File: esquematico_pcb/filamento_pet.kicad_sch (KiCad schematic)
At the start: 35 parts, among them P1 Digital, P2 Analog, P3 CONN_01X01, P4 CONN_01X01, P5 CONN_01X01, P6 CONN_01X01, Q1 IRF540N, Q2 IRF540N

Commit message: Footprints listos
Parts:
- removed J? (x3): Conn_01x02_Male, symbol filamento_pet-rescue:Conn_01x02_Male-Connector
- removed J? (x4): 01x02M, symbol filamento_pet-rescue:Conn_01x02_Male-Connector
- removed P3, P4, P5, P6: CONN_01X01, Socket_Arduino_Nano:1pin_Nano, symbol Connector_Generic:Conn_01x01
- added J1, J11, J13, J2, J4, J5, J8: 01x02M, TerminalBlock_4Ucon:TerminalBlock_4Ucon_1x02_P3.50mm_Horizontal, symbol filamento_pet-rescue:Conn_01x02_Male-Connector
- C1, C3: value CP1 -> 100uf; footprint (none) -> Capacitor_THT:CP_Radial_D8.0mm_P3.50mm
- C2: value CP1 -> 10uf; footprint (none) -> Capacitor_THT:CP_Radial_D8.0mm_P3.50mm
- D1, D2: footprint (none) -> LED_THT:LED_D5.0mm
- J10, J6, J7: renamed from J?; footprint (none) -> Connector_PinHeader_2.54mm:PinHeader_1x03_P2.54mm_Vertical
- J12, J9: renamed from J?; footprint (none) -> Connector_PinHeader_2.54mm:PinHeader_1x04_P2.54mm_Vertical
- J3: renamed from J?; footprint (none) -> TerminalBlock_4Ucon:TerminalBlock_4Ucon_1x02_P3.50mm_Horizontal
- P1, P2: footprint Socket_Arduino_Nano:Socket_Strip_Arduino_1x15 -> Connector_PinHeader_2.54mm:PinHeader_1x16_P2.54mm_Vertical
- R1, R2, R3, R4, R5, R6, R7: footprint (none) -> Resistor_THT:R_Axial_DIN0204_L3.6mm_D1.6mm_P7.62mm_Horizontal
- R8: value 10K -> R; footprint (none) -> Resistor_THT:R_Axial_DIN0204_L3.6mm_D1.6mm_P7.62mm_Horizontal
- gave numbers to parts that had none: 1
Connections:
- net +12V: now also J2.1 (Pin_1), J5.2 (Pin_2)
- net +5V: now also R7.2, R8.1; no longer R7.1, R8.2
- net BUT1: now also J8.2 (Pin_2)
- net BUT2: now also J11.2 (Pin_2)
- net BUT3: now also J13.2 (Pin_2)
- net EN: now also R8.2; no longer R8.1
- net FAN: now also R5.2; no longer R5.1
- net GND: now also R3.2, R6.2, J1.2 (Pin_2), J11.1 (Pin_1), J13.1 (Pin_1), J4.2 (Pin_2), J8.1 (Pin_1); no longer R3.1, R6.1
- net MOS: now also R2.2; no longer R2.1
- net Thermistor: now also R7.1, J4.1 (Pin_1); no longer R7.2
- net at D2.1 (K), Q2.2 (D): now also J5.1 (Pin_1)
- new net: Q1.1 (G), R2.1, R3.1
- new net: Q2.1 (G), R5.1, R6.1
- new net: J1.1 (Pin_1), J2.2 (Pin_2)
- no-connect marks 3 -> 0
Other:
- note removed: "Holes"

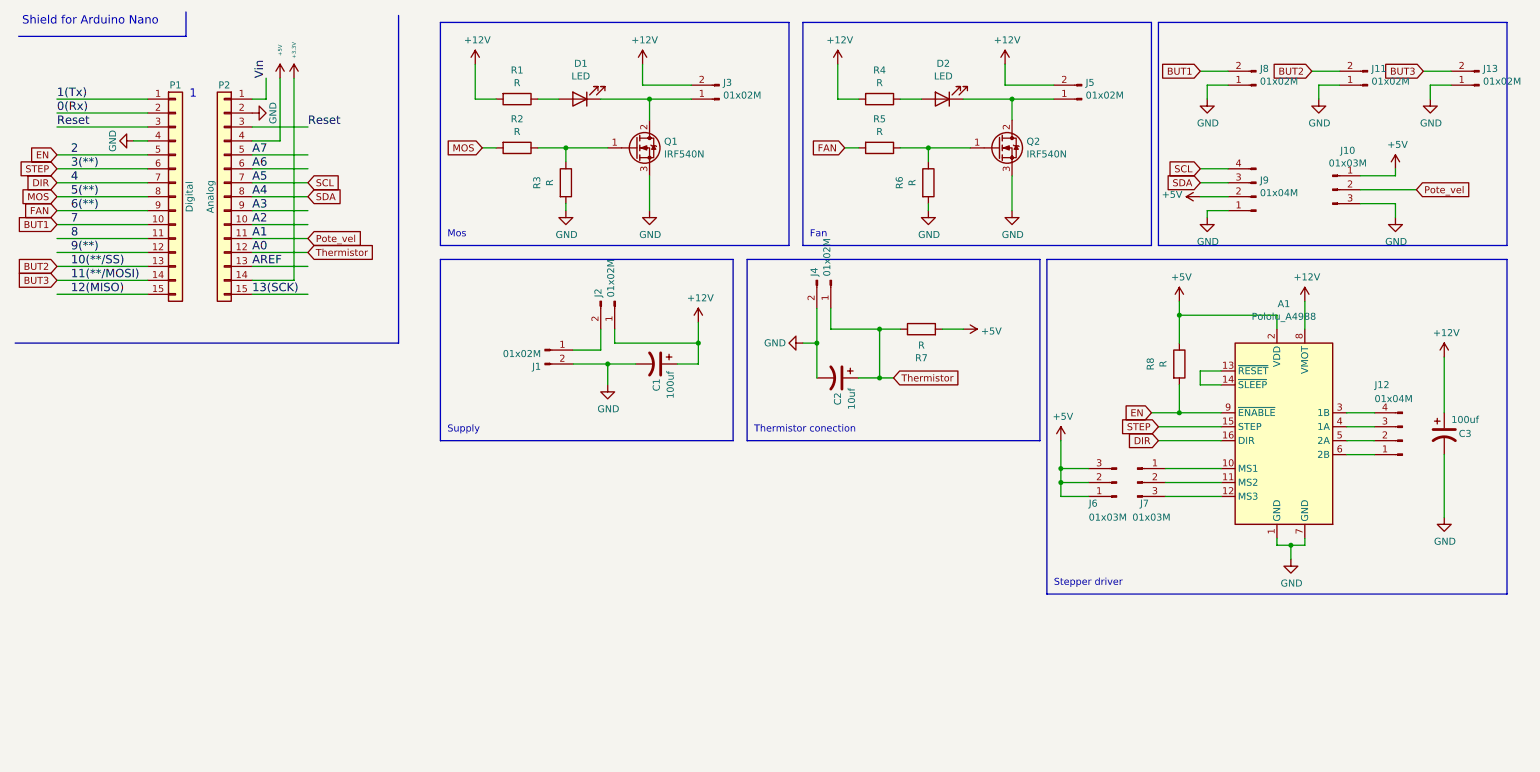
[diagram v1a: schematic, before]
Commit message: Cambio de footprint Arduino Nano. Conector para encoder (Opcional). 2 Botones
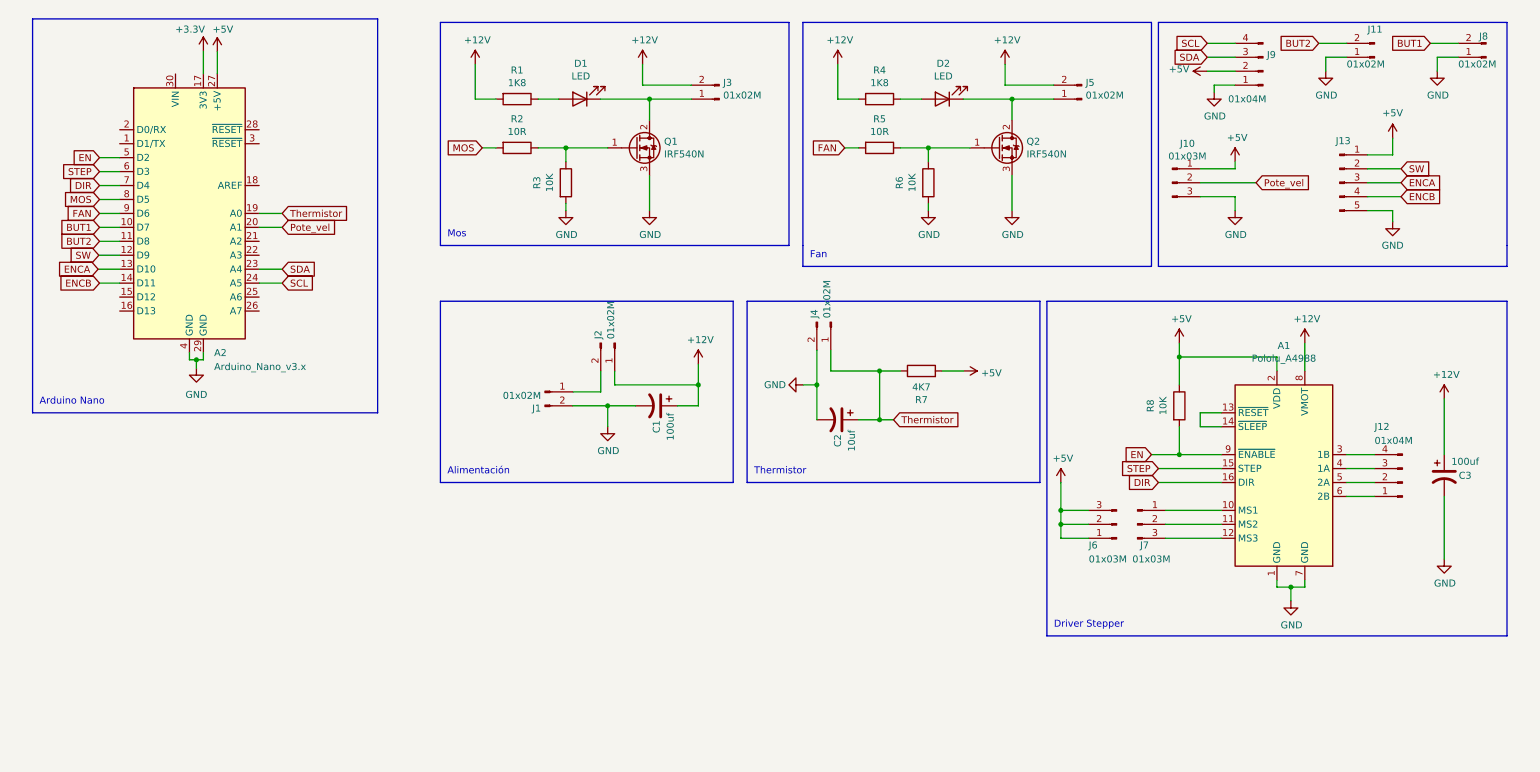
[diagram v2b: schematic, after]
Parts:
- removed J13: 01x02M, TerminalBlock_4Ucon:TerminalBlock_4Ucon_1x02_P3.50mm_Horizontal, symbol filamento_pet-rescue:Conn_01x02_Male-Connector
- removed P1: Digital, Connector_PinHeader_2.54mm:PinHeader_1x16_P2.54mm_Vertical, symbol Connector_Generic:Conn_01x15
- removed P2: Analog, Connector_PinHeader_2.54mm:PinHeader_1x16_P2.54mm_Vertical, symbol Connector_Generic:Conn_01x15
- added A2: Arduino_Nano_v3.x, Module:Arduino_Nano, symbol MCU_Module:Arduino_Nano_v3.x
- added J13: Conn_01x05_Pin, Connector_PinHeader_2.54mm:PinHeader_1x05_P2.54mm_Vertical, symbol Connector:Conn_01x05_Pin
- R1, R4: value R -> 1K8
- R2, R5: value R -> 10R
- R3, R6, R8: value R -> 10K
- R7: value R -> 4K7
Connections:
- net +5V: now also A2.27 (+5V), J13.1 (Pin_1)
- net BUT1: now also A2.10 (D7)
- net BUT2: now also A2.11 (D8)
- net DIR: now also A2.7 (D4)
- net EN: now also A2.5 (D2)
- net FAN: now also A2.9 (D6)
- net GND: now also A2.29 (GND), A2.4 (GND), J13.5 (Pin_5)
- net MOS: now also A2.8 (D5)
- net Pote_vel: now also A2.20 (A1)
- net SCL: now also A2.24 (A5)
- net SDA: now also A2.23 (A4)
- net STEP: now also A2.6 (D3)
- net Thermistor: now also A2.19 (A0)
- new net +3.3V: A2.17 (3V3)
- new net ENCA: A2.13 (D10), J13.3 (Pin_3)
- new net ENCB: A2.14 (D11), J13.4 (Pin_4)
- new net SW: A2.12 (D9), J13.2 (Pin_2)
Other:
- note added: "Alimentación"
- note added: "Arduino Nano"
- note added: "Driver Stepper"
- note added: "Thermistor"
- note removed: "1"
- note removed: "Shield for Arduino Nano"
- note removed: "Stepper driver"
- note removed: "Supply"
- note removed: "Thermistor conection"
- moved on the sheet: A1, C1, C2, C3, J1, J10, J11, J12, J2, J4, J6, J7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

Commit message: PCB V1.0.0
Agregué LM7805
Cambios pequeños en el esquemático
V1.0.0 del PCB
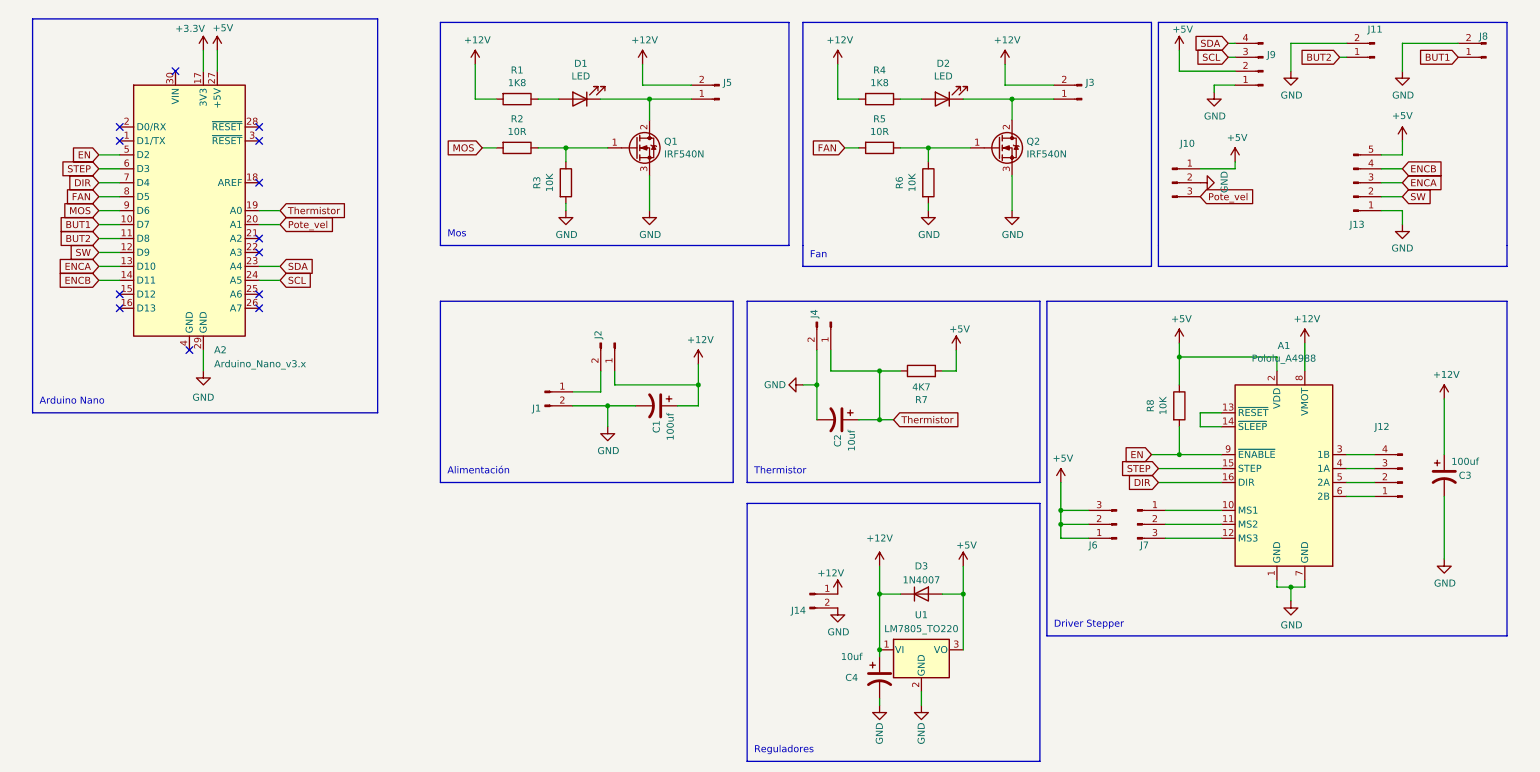
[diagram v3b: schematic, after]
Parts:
- added C4: 10uf, Capacitor_THT:CP_Radial_D8.0mm_P3.50mm, symbol filamento_pet-rescue:CP1-Device
- added D3: 1N4007, Diode_THT:D_DO-41_SOD81_P10.16mm_Horizontal, symbol Diode:1N4007
- added J14: 01x02M, TerminalBlock_4Ucon:TerminalBlock_4Ucon_1x02_P3.50mm_Horizontal, symbol filamento_pet-rescue:Conn_01x02_Male-Connector
- added U1: LM7805_TO220, Package_TO_SOT_THT:TO-220-3_Vertical, symbol Regulator_Linear:LM7805_TO220
- renumbered J5 to J3, J3 to J5
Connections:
- net +12V: now also C4.1, D3.1 (K), J14.1 (Pin_1), U1.1 (VI)
- net +5V: now also J13.5 (Pin_5), D3.2 (A), U1.3 (VO); no longer J13.1 (Pin_1)
- net BUT1: now also J8.1 (Pin_1); no longer J8.2 (Pin_2)
- net BUT2: now also J11.1 (Pin_1); no longer J11.2 (Pin_2)
- net FAN: now also A2.8 (D5); no longer A2.9 (D6)
- net GND: now also J10.2 (Pin_2), J11.2 (Pin_2), J13.1 (Pin_1), J8.2 (Pin_2), C4.2, J14.2 (Pin_2), U1.2 (GND); no longer A2.4 (GND), J10.3 (Pin_3), J11.1 (Pin_1), J13.5 (Pin_5), J8.1 (Pin_1)
- net MOS: now also A2.9 (D6); no longer A2.8 (D5)
- net Pote_vel: now also J10.3 (Pin_3); no longer J10.2 (Pin_2)
- net SCL: now also J9.3 (Pin_3); no longer J9.4 (Pin_4)
- net SDA: now also J9.4 (Pin_4); no longer J9.3 (Pin_3)
- no-connect marks 0 -> 13
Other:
- note added: "Reguladores"
- moved on the sheet: A2, J13
